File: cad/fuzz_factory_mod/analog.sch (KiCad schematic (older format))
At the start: 14 parts

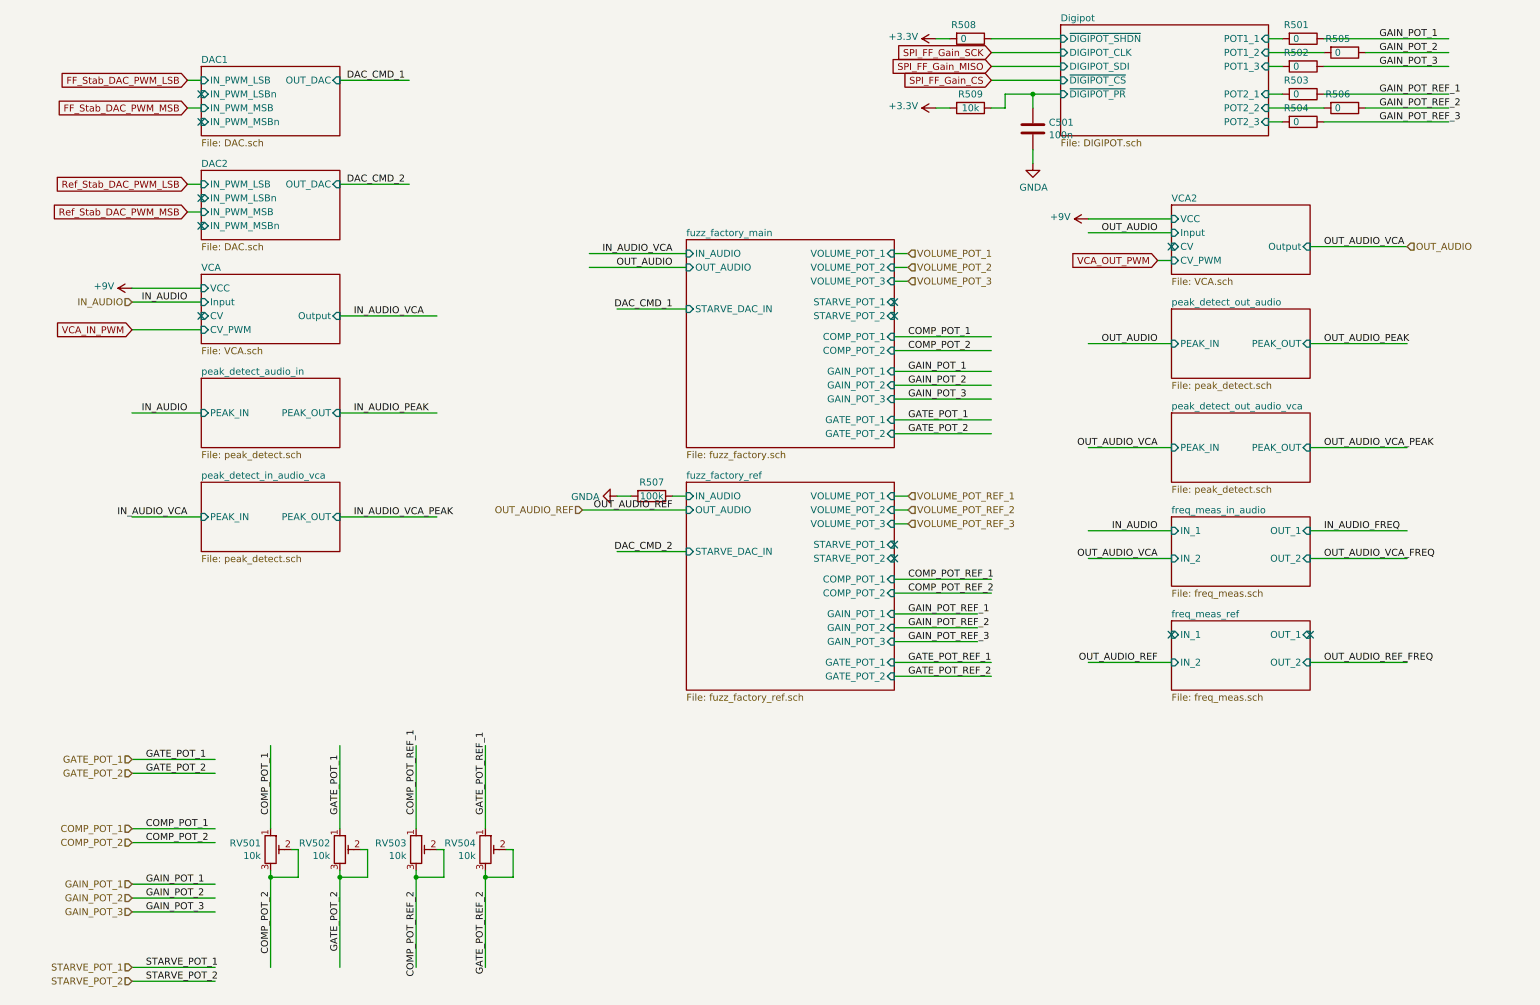
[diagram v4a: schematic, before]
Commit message: Continued schematic.
Continued component placement.
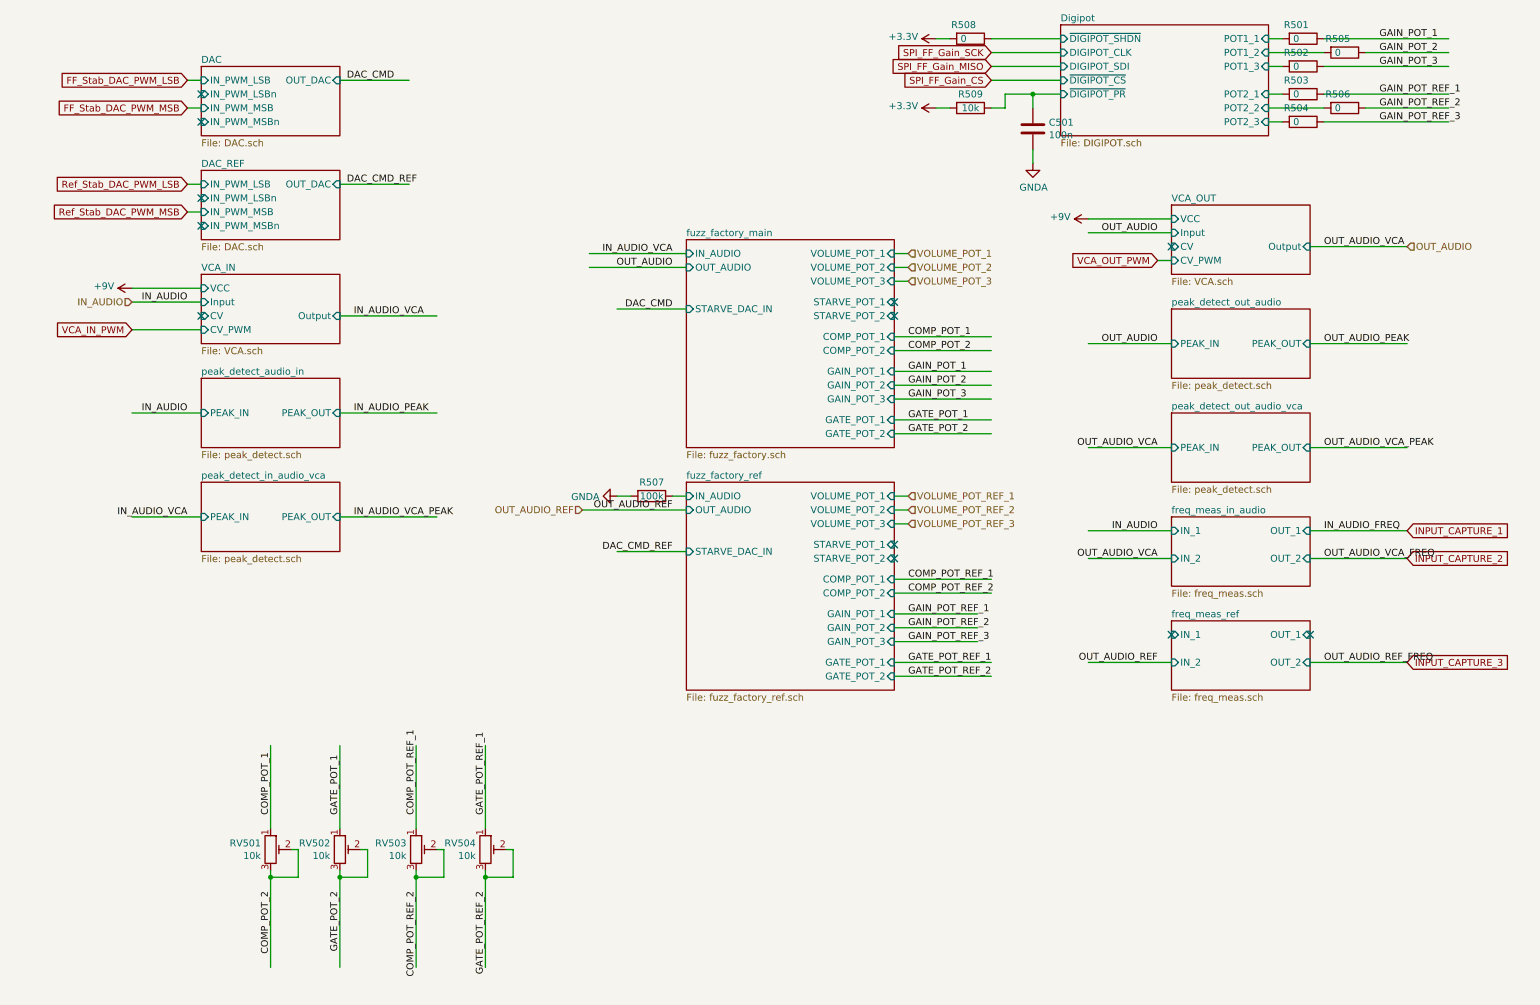
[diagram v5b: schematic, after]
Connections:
- net labels added: DAC_CMD, DAC_CMD_REF, INPUT_CAPTURE_1, INPUT_CAPTURE_2, INPUT_CAPTURE_3
- net labels removed: DAC_CMD_1, DAC_CMD_2, STARVE_POT_1, STARVE_POT_2
- wire segments 112 -> 103
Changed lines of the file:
@@
 $Descr A4 11693 8268
 encoding utf-8
-Sheet 5 30
+Sheet 13 30
 Title ""
 Date ""
@@
 S 2000 1000 1000 500
 U 5DF28E5E
-F0 "DAC1" 50
+F0 "DAC" 50
 F1 "DAC.sch" 50
 F2 "IN_PWM_LSB" I L 2000 1100 50
@@
 $EndSheet
 Text Label 5400 2750 2    50   ~ 0
-DAC_CMD_1
+DAC_CMD
 Text Label 3050 1100 0    50   ~ 0
-DAC_CMD_1
+DAC_CMD
 Wire Wire Line
 	3000 1100 3500 1100
-Text HLabel 1500 6900 0    50   Input ~ 0
-GAIN_POT_1
-Text HLabel 1500 7000 0    50   Input ~ 0
-GAIN_POT_2
-Text HLabel 1500 7100 0    50   Input ~ 0
-GAIN_POT_3
-Text HLabel 1500 6500 0    50   Input ~ 0
-COMP_POT_1
-Text HLabel 1500 6600 0    50   Input ~ 0
-COMP_POT_2
 Text HLabel 7100 2350 2    50   Input ~ 0
 VOLUME_POT_1
@@
 Text HLabel 7100 2550 2    50   Input ~ 0
 VOLUME_POT_3
-Text HLabel 1500 6000 0    50   Input ~ 0
-GATE_POT_1
-Text HLabel 1500 6100 0    50   Input ~ 0
-GATE_POT_2
 $Comp
 L Device:R_POT_TRIM RV501
@@
 Text Label 3000 6950 3    50   ~ 0
 GATE_POT_2
-Text Label 1600 6000 0    50   ~ 0
-GATE_POT_1
-Text Label 1600 6100 0    50   ~ 0
-GATE_POT_2
-Text Label 1600 6500 0    50   ~ 0
-COMP_POT_1
-Text Label 1600 6600 0    50   ~ 0
-COMP_POT_2
-Text Label 1600 6900 0    50   ~ 0
-GAIN_POT_1
-Text Label 1600 7000 0    50   ~ 0
-GAIN_POT_2
-Text Label 1600 7100 0    50   ~ 0
-GAIN_POT_3
-Wire Wire Line
-	1500 6000 2100 6000
-Wire Wire Line
-	1500 6100 2100 6100
-Wire Wire Line
-	1500 6500 2100 6500
-Wire Wire Line
-	1500 6600 2100 6600
-Wire Wire Line
-	1500 6900 2100 6900
-Wire Wire Line
-	1500 7000 2100 7000
-Wire Wire Line
-	1500 7100 2100 7100
 Wire Wire Line
 	2500 6850 2500 7500
@@
 Wire Wire Line
 	3000 6500 3000 5900
-Text Label 1600 7500 0    50   ~ 0
-STARVE_POT_1
-Text Label 1600 7600 0    50   ~ 0
-STARVE_POT_2
-Text HLabel 1500 7500 0    50   Input ~ 0
-STARVE_POT_1
-Text HLabel 1500 7600 0    50   Input ~ 0
-STARVE_POT_2
-Wire Wire Line
-	1500 7500 2100 7500
-Wire Wire Line
-	1500 7600 2100 7600
 $Sheet
 S 8200 700  1500 800
@@
 S 2000 2500 1000 500
 U 5E344810
-F0 "VCA" 50
+F0 "VCA_IN" 50
 F1 "VCA.sch" 50
 F2 "CV" I L 2000 2800 50
@@
 S 9000 2000 1000 500
 U 5E6FC466
-F0 "VCA2" 50
+F0 "VCA_OUT" 50
 F1 "VCA.sch" 50
 F2 "CV" I L 9000 2300 50
@@
 S 2000 1750 1000 500
 U 5ED499CE
-F0 "DAC2" 50
+F0 "DAC_REF" 50
 F1 "DAC.sch" 50
 F2 "IN_PWM_LSB" I L 2000 1850 50
@@
 $EndSheet
 Text Label 3050 1850 0    50   ~ 0
-DAC_CMD_2
+DAC_CMD_REF
 Wire Wire Line
 	3000 1850 3500 1850
@@
 NoConn ~ 2000 2150
 Text Label 5400 4500 2    50   ~ 0
-DAC_CMD_2
+DAC_CMD_REF
 Wire Wire Line
 	5500 4500 5000 4500
@@
 NoConn ~ 10000 5100
 NoConn ~ 9000 5100
+Text GLabel 10700 4350 2    50   Input ~ 0
+INPUT_CAPTURE_1
+Text GLabel 10700 4550 2    50   Input ~ 0
+INPUT_CAPTURE_2
+Text GLabel 10700 5300 2    50   Input ~ 0
+INPUT_CAPTURE_3
 $EndSCHEMATC

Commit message: Commit pre- board separation.
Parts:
- added J1301: Conn_analog_1, Pin_Headers:Pin_Header_Straight_1x06_Pitch2.54mm, symbol Connector:Conn_01x06_Female
- added J1302: Conn_analog_2, Pin_Headers:Pin_Header_Straight_1x06_Pitch2.54mm, symbol Connector:Conn_01x06_Female
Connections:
- net labels added: IN_AUDIO_REF
- wire segments 103 -> 113
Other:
- moved on the sheet: R507

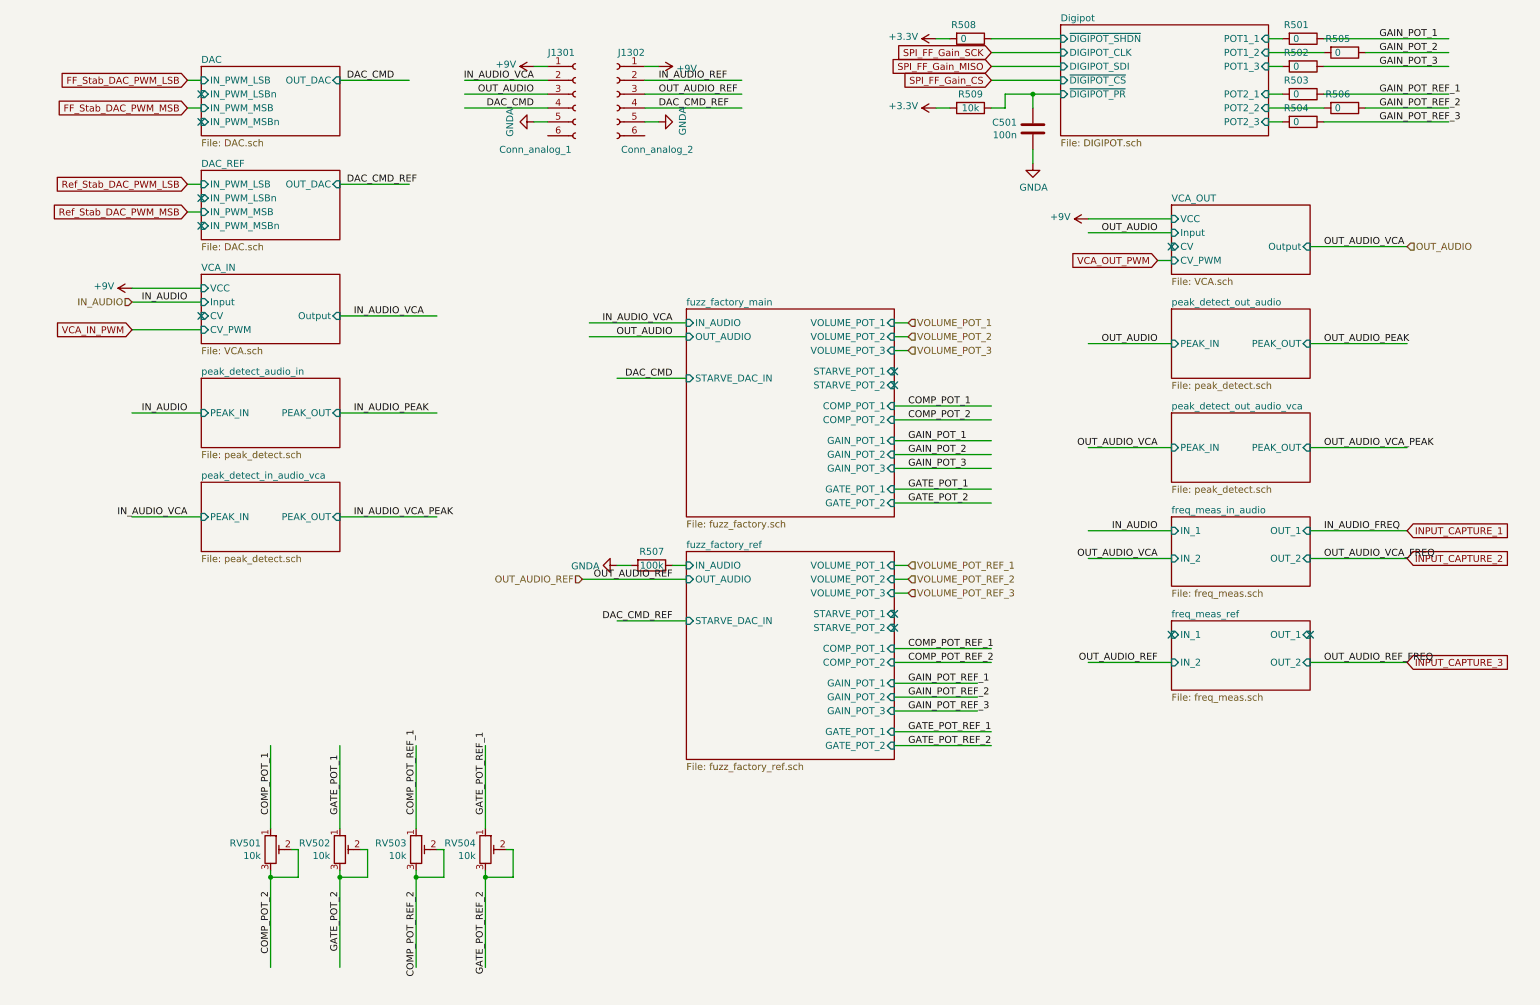
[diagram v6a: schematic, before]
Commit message: Changes architecture.
Corrections on schematic.
Continued Layout placement.
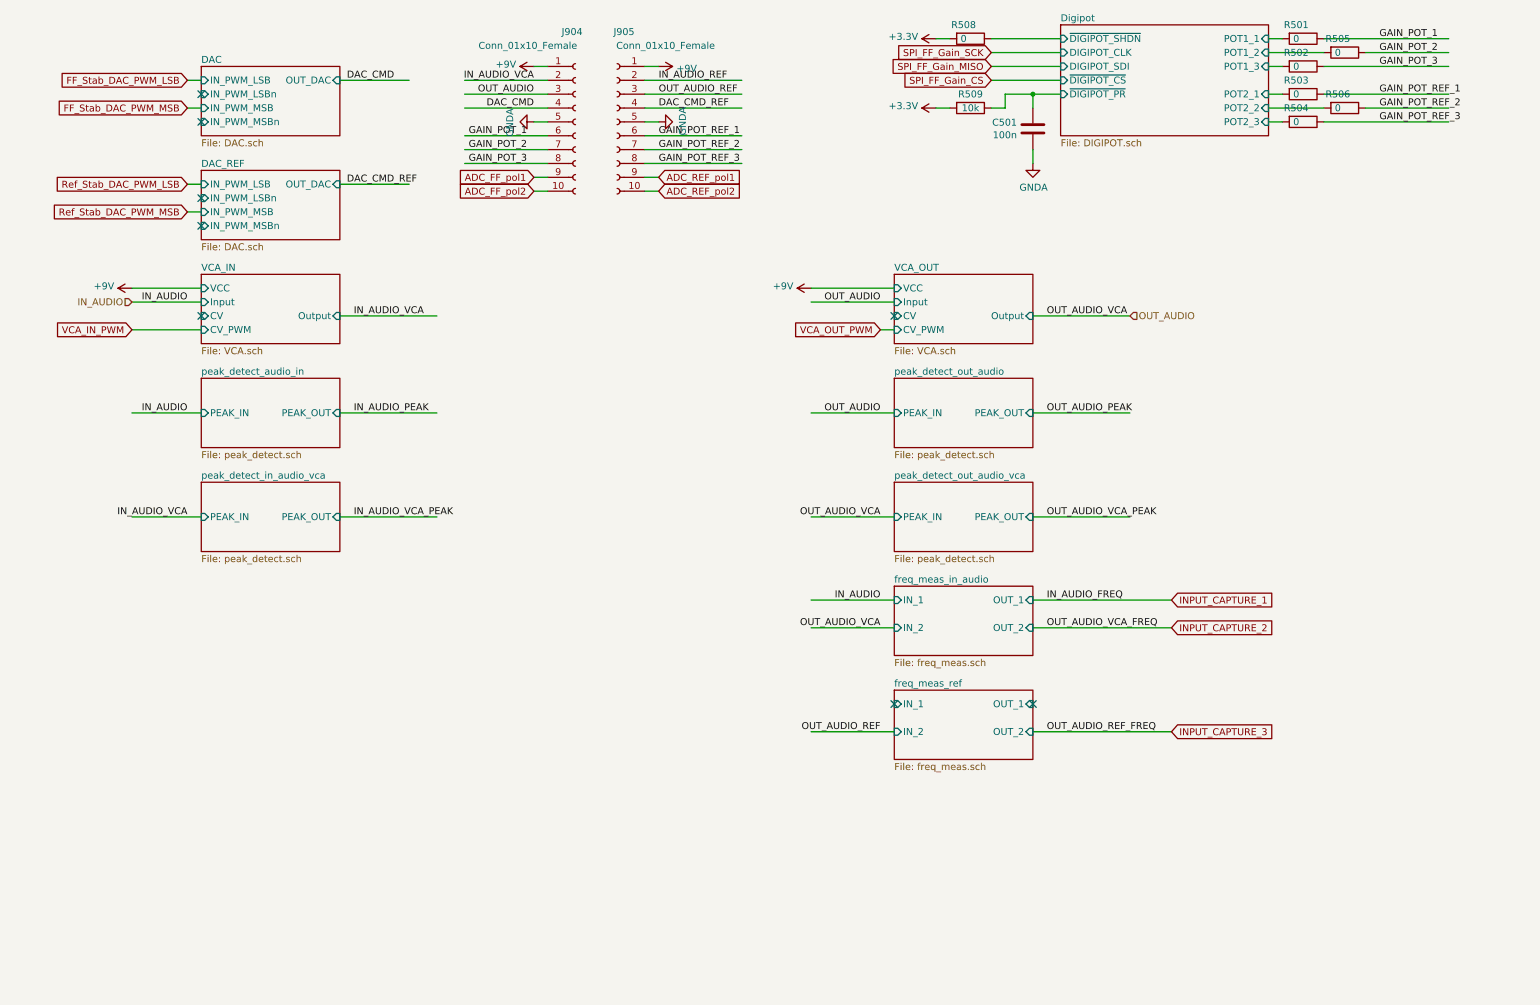
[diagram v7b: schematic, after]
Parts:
- removed J1301: Conn_analog_1, Pin_Headers:Pin_Header_Straight_1x06_Pitch2.54mm, symbol Connector:Conn_01x06_Female
- removed J1302: Conn_analog_2, Pin_Headers:Pin_Header_Straight_1x06_Pitch2.54mm, symbol Connector:Conn_01x06_Female
- removed R507: 100k, Resistors_SMD:R_0603, symbol Device:R
- removed RV501, RV502, RV503, RV504: 10k, Potentiometers:Potentiometer_Trimmer_Bourns_3266X, symbol Device:R_POT_TRIM
- added J904, J905: Conn_01x10_Female, Pin_Headers:Pin_Header_Straight_1x10_Pitch2.54mm, symbol Connector:Conn_01x10_Female
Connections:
- net labels added: ADC_FF_pol1, ADC_FF_pol2, ADC_REF_pol1, ADC_REF_pol2
- net labels removed: COMP_POT_1, COMP_POT_2, COMP_POT_REF_1, COMP_POT_REF_2, GATE_POT_1, GATE_POT_2, GATE_POT_REF_1, GATE_POT_REF_2, VOLUME_POT_1, VOLUME_POT_2, VOLUME_POT_3, VOLUME_POT_REF_1, VOLUME_POT_REF_2, VOLUME_POT_REF_3
- wire segments 113 -> 72
- no-connect marks 12 -> 8
